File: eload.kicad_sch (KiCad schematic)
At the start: 23 parts, among them J1 Device Power, J2 Input Power, J3 SWD Header, Q1 TIP122, SW1 RotaryEncoder_Switch, U1 STM32F103C8T6, U2 LM1117DT-3.3, U3 AD8629, U4 MCP4725

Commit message: WIP schematic
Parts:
- added C7, C8: C_Small, symbol Device:C_Small
- added C9: 10uF, symbol Device:C_Polarized_Small
- added R10, R5, R9: 10K, symbol Device:R_Small
- added R6: 90K, symbol Device:R_Small
- added Y1: Crystal, symbol Device:Crystal
- R2: value 330K -> 40K
- R3: value 100K -> 10K
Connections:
- net +3.3V: now also C9.1, R10.1, R9.1
- net GND: now also U1.44 (BOOT0), C7.2, C8.2, C9.2, R5.2
- net SCL: now also R9.2
- net SDA: now also R10.2
- net Vctrl: now also R5.1, R6.1; no longer U4.1 (VOUT)
- net OSC1: now reaches U1.5 (PD0)
- net OSC1: now also C8.1, Y1.1
- net OSC2: now reaches U1.6 (PD1)
- net OSC2: now also C7.1, Y1.2
- new net: R6.2, U4.1 (VOUT)
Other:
- note added: "15V MAX 12bit ADC 1bit/mV = 4.096V 5x attenuation on Vsense (15V to 3V)"
- note added: "1A * 0.1R = 0.1V"
- note added: "1V = 1A 10x attenuation"
- note removed: "15V MAX 12bit ADC 1bit/mV = 4.096V 1:4 division"
- moved on the sheet: C1, C5, C6, U1, U4

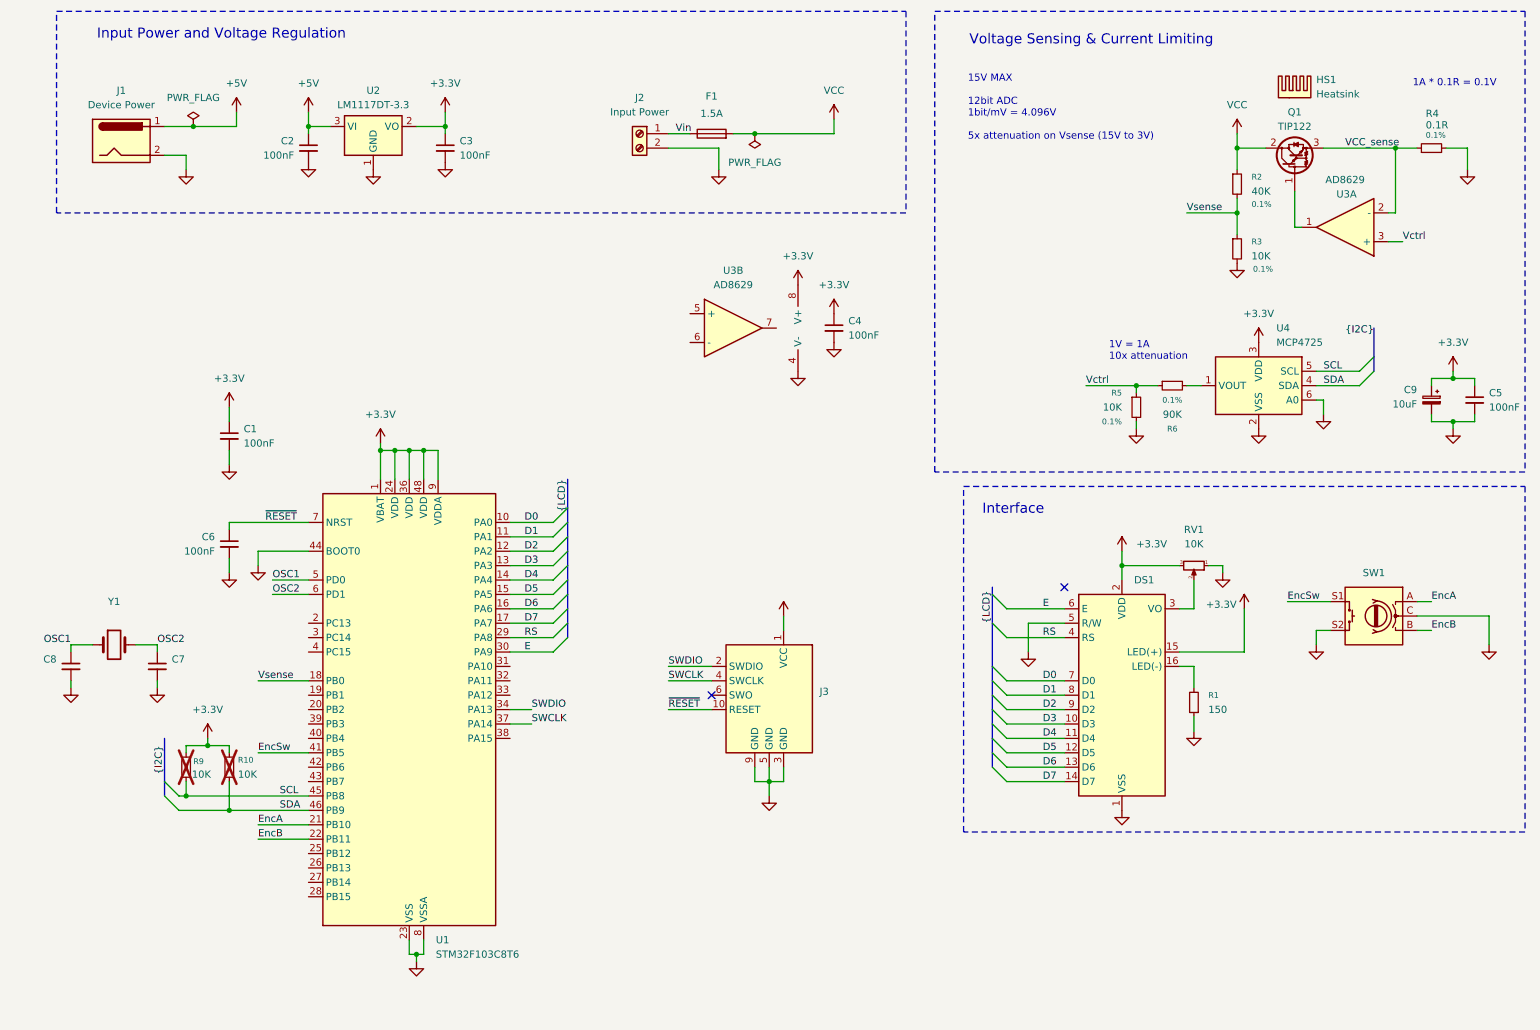
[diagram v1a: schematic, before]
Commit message: Update footprints
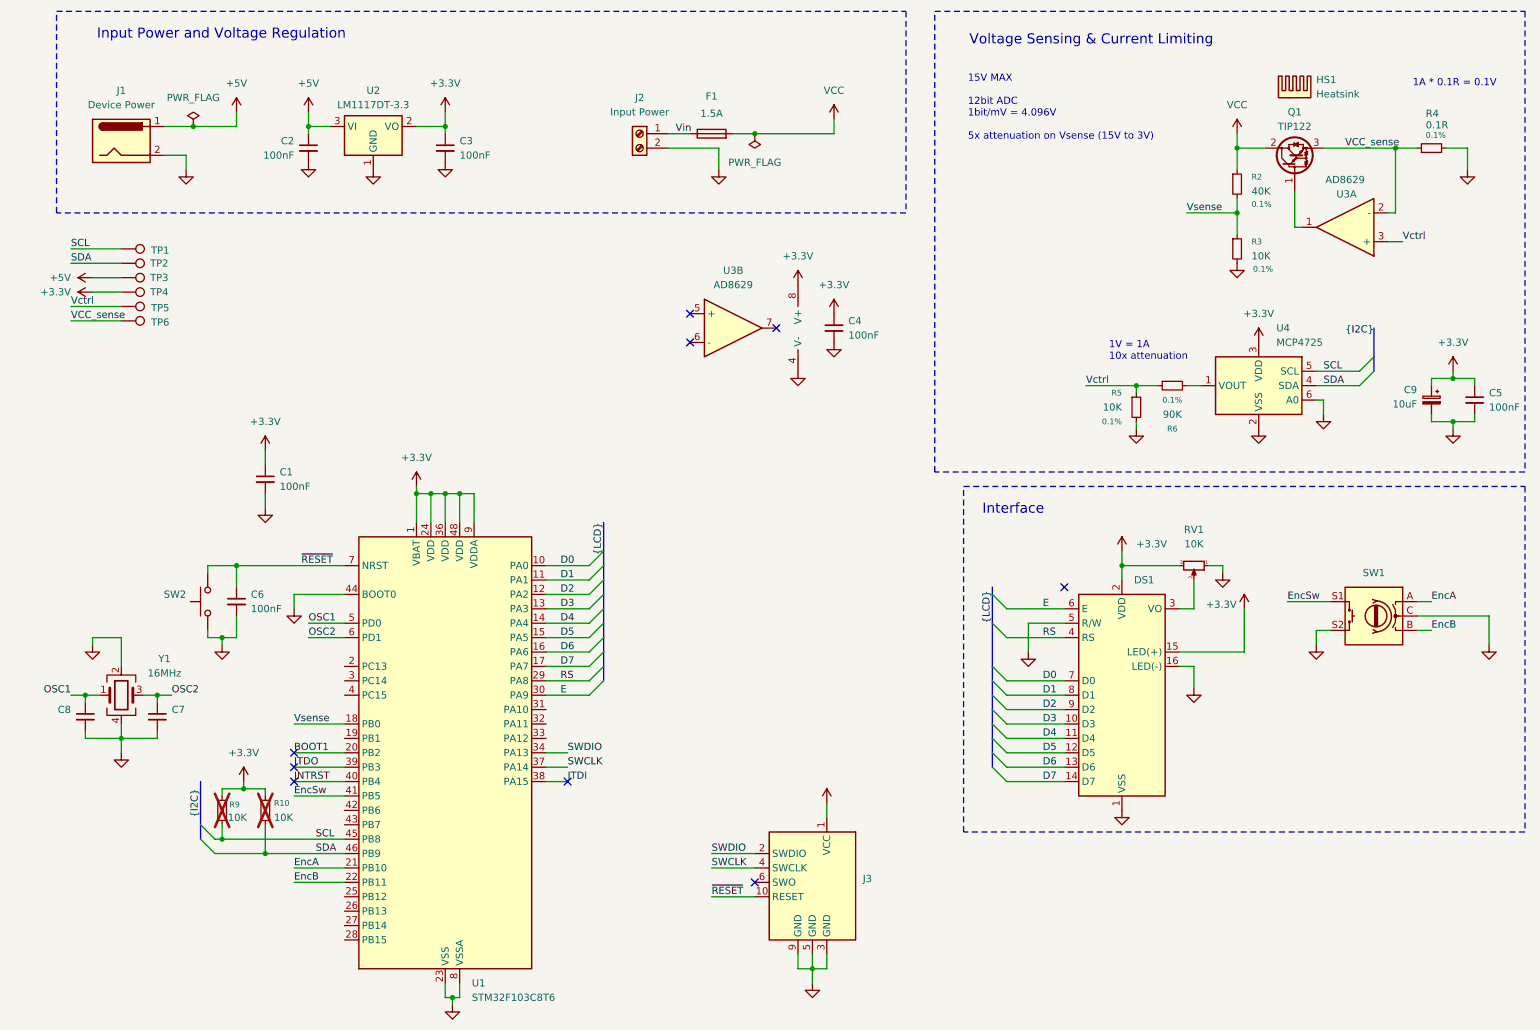
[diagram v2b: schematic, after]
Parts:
- removed R1: 150, symbol Device:R_Small
- removed Y1: Crystal, symbol Device:Crystal
- added SW2: SW_Push, symbol Switch:SW_Push
- added TP1, TP2, TP3, TP4, TP5, TP6: TestPoint, symbol Connector:TestPoint
- added Y1: 16MHz, Crystal:Crystal_SMD_3225-4Pin_3.2x2.5mm_HandSoldering, symbol Device:Crystal_GND24
- C1, C2, C3, C4, C5, C6, C7, C8: footprint (none) -> Capacitor_SMD:C_0805_2012Metric_Pad1.18x1.45mm_HandSolder
- C9: footprint (none) -> Capacitor_Tantalum_SMD:CP_EIA-3216-18_Kemet-A_HandSolder
- U3: footprint (none) -> Package_SO:SOP-8_3.76x4.96mm_P1.27mm; LCSC Part # C47411541 -> C47411543
- U4: LCSC Part # (none) -> C144198
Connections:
- net +3.3V: now also TP4.1
- net +5V: now also TP3.1
- net GND: now also DS1.16 (LED(-)), SW2.1, Y1.2, Y1.4
- net OSC1: now also Y1.1
- net OSC2: now also Y1.3
- net SCL: now also TP1.1
- net SDA: now also TP2.1
- net VCC_sense: now also TP6.1
- net Vctrl: now also TP5.1
- net ~{RESET}: now also SW2.2
- net BOOT1: now reaches U1.20 (PB2)
- net JTDI: now reaches U1.38 (PA15)
- net JTDO: now reaches U1.39 (PB3)
- net JNTRST: now reaches U1.40 (PB4)
- no-connect marks 2 -> 9
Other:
- moved on the sheet: C1, C6, C7, C8, J3, R10, R9, U1

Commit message: WIP
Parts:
- added J3, J6: Conn_01x16_Socket, Connector_JST:JST_XH_B16B-XH-A_1x16_P2.50mm_Vertical, symbol Connector:Conn_01x16_Socket
- added J5: Conn_01x14_Pin, Connector_PinHeader_2.54mm:PinHeader_2x07_P2.54mm_Vertical, symbol Connector:Conn_01x14_Pin
- added TP7: TestPoint, TestPoint:TestPoint_Loop_D1.80mm_Drill1.0mm_Beaded, symbol Connector:TestPoint
- C1: renamed from C8; value C_Small -> 20pF; LCSC Part # (none) -> C149606
- C2: renamed from C7; value C_Small -> 20pF; LCSC Part # (none) -> C149606
- C3: renamed from C6; LCSC Part # (none) -> C49678
- C4: renamed from C1; LCSC Part # (none) -> C49678
- C5: renamed from C2; LCSC Part # (none) -> C49678
- C6: renamed from C3; LCSC Part # (none) -> C49678
- C7: renamed from C4; LCSC Part # (none) -> C49678
- C8: renamed from C9; LCSC Part # (none) -> C110055
- C9: renamed from C5; LCSC Part # (none) -> C49678
- DS1: now left out of the parts list
- J1: footprint Connector_BarrelJack:BarrelJack_SwitchcraftConxall_RAPC10U_Horizontal -> Connector_BarrelJack:BarrelJack_Horizontal; LCSC Part # (none) -> C7498153
- J2: value Input Power -> Input; footprint (none) -> TerminalBlock_CUI:TerminalBlock_CUI_TB007-508-02_1x02_P5.08mm_Horizontal; LCSC Part # (none) -> C8465
- Q1: LCSC Part # C16283 -> C3816270
- R1: renamed from R9; footprint (none) -> Resistor_SMD:R_0805_2012Metric_Pad1.20x1.40mm_HandSolder; LCSC Part # (none) -> C110775
- R2: renamed from R10; footprint (none) -> Resistor_SMD:R_0805_2012Metric_Pad1.20x1.40mm_HandSolder; LCSC Part # (none) -> C110775
- R3: renamed from R5; footprint (none) -> Resistor_SMD:R_0805_2012Metric_Pad1.20x1.40mm_HandSolder; LCSC Part # (none) -> C110775
- R4: renamed from R6; footprint (none) -> Resistor_SMD:R_0805_2012Metric_Pad1.20x1.40mm_HandSolder
- R5: renamed from R2; footprint (none) -> Resistor_SMD:R_0805_2012Metric_Pad1.20x1.40mm_HandSolder; LCSC Part # (none) -> C865475
- R6: renamed from R3; footprint (none) -> Resistor_SMD:R_0805_2012Metric_Pad1.20x1.40mm_HandSolder; LCSC Part # (none) -> C110775
- R7: renamed from R4; footprint (none) -> Resistor_SMD:R_1206_3216Metric_Pad1.30x1.75mm_HandSolder; LCSC Part # (none) -> C7467250
- RV1: footprint (none) -> Potentiometer_THT:Potentiometer_Bourns_3266W_Vertical; LCSC Part # (none) -> C49241482
- SW2: renamed from SW1; footprint (none) -> Rotary_Encoder:RotaryEncoder_Bourns_Vertical_PEC12R-3x17F-Sxxxx; LCSC Part # (none) -> C5331618
- TP1, TP2, TP3, TP4, TP5, TP6: footprint (none) -> TestPoint:TestPoint_Pad_D1.5mm
- U1: renamed from U2; footprint Package_TO_SOT_SMD:TO-252-2 -> Package_TO_SOT_SMD:SOT-223; LCSC Part # (none) -> C126027
- renumbered J3 to J4, SW2 to SW1, U1 to U2
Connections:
- net +3.3V: now also J3.16 (Pin_16), J6.16 (Pin_16)
- net D0: now also J3.15 (Pin_15), J6.15 (Pin_15)
- net D1: now also J3.14 (Pin_14), J6.14 (Pin_14)
- net D2: now also J3.13 (Pin_13), J6.13 (Pin_13)
- net D3: now also J3.12 (Pin_12), J6.12 (Pin_12)
- net D4: now also J3.11 (Pin_11), J6.11 (Pin_11)
- net D5: now also J3.10 (Pin_10), J6.10 (Pin_10)
- net D6: now also J3.9 (Pin_9), J6.9 (Pin_9)
- net D7: now also J3.8 (Pin_8), J6.8 (Pin_8)
- net E: now also J3.7 (Pin_7), J6.7 (Pin_7)
- net EncA: now also J3.3 (Pin_3), J6.3 (Pin_3)
- net EncB: now also J3.2 (Pin_2), J6.2 (Pin_2)
- net EncSw: now also J3.4 (Pin_4), J6.4 (Pin_4)
- net GND: now also J3.1 (Pin_1), J5.1 (Pin_1), J6.1 (Pin_1), TP7.1
- net RS: now also J3.6 (Pin_6), J6.6 (Pin_6)
- net PB1: now reaches U2.19 (PB1)
- net PB1: now also J5.8 (Pin_8)
- net PC13: now reaches U2.2 (PC13)
- net PC13: now also J5.5 (Pin_5)
- net PB12: now reaches U2.25 (PB12)
- net PB12: now also J5.11 (Pin_11)
- net PB13: now reaches U2.26 (PB13)
- net PB13: now also J5.12 (Pin_12)
- net PB14: now reaches U2.27 (PB14)
- net PB14: now also J5.13 (Pin_13)
- net PB15: now reaches U2.28 (PB15)
- net PB15: now also J5.14 (Pin_14)
- net PC14: now reaches U2.3 (PC14)
- net PC14: now also J5.6 (Pin_6)
- net PA10: now reaches U2.31 (PA10)
- net PA10: now also J5.4 (Pin_4)
- net PA11: now reaches U2.32 (PA11)
- net PA11: now also J5.3 (Pin_3)
- net PA12: now reaches U2.33 (PA12)
- net PA12: now also J5.2 (Pin_2)
- net PC15: now reaches U2.4 (PC15)
- net PC15: now also J5.7 (Pin_7)
- net PB6: now reaches U2.42 (PB6)
- net PB6: now also J5.9 (Pin_9)
- net PB7: now reaches U2.43 (PB7)
- net PB7: now also J5.10 (Pin_10)
- no-connect marks 9 -> 10
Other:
- moved on the sheet: DS1, RV1, SW2, TP1, TP2, TP3, TP4, TP5, TP6

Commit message: WIP
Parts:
- F1: footprint (none) -> Resistor_THT:R_Axial_DIN0204_L3.6mm_D1.6mm_P7.62mm_Horizontal
- HS1: LCSC Part # (none) -> C4657
- J3, J6: value Conn_01x16_Socket -> JST Header; LCSC Part # (none) -> C158022
- J5: value Conn_01x14_Pin -> ~; LCSC Part # (none) -> C41413844
- R4: value 90K -> 89.8K; LCSC Part # (none) -> C865684
- U2: value STM32F103C8T6 -> STM32F103CBT6; LCSC Part # (none) -> C8734
- U3: footprint Package_SO:SOP-8_3.76x4.96mm_P1.27mm -> Package_SO:JEITA_SOIC-8_3.9x4.9mm_P1.27mm; LCSC Part # C47411543 -> C653045
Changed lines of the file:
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@@
 			)
 		)
-		(property "Datasheet" "~"
+		(property "Datasheet" "https://www.lcsc.com/datasheet/C4657.pdf"
 			(at 236.5248 33.02 0)
 			(effects
@@
 			)
 		)
+		(property "LCSC Part #" "C4657"
+			(at 236.22 33.02 0)
+			(effects
+				(font
+					(size 1.27 1.27)
+				)
+				(hide yes)
+			)
+		)
 		(instances
 			(project ""
@@
 			)
 		)
-		(property "Value" "Conn_01x16_Socket"
+		(property "Value" "JST Header"
 			(at 146.05 124.4599 0)
 			(effects
@@
 			)
 		)
-		(property "Datasheet" "~"
+		(property "Datasheet" "https://www.lcsc.com/datasheet/C158022.pdf"
 			(at 144.78 121.92 0)
 			(effects
@@
 			)
 		)
+		(property "LCSC Part #" "C158022"
+			(at 144.78 121.92 0)
+			(effects
+				(font
+					(size 1.27 1.27)
+				)
+				(hide yes)
+			)
+		)
 		(pin "2"
 		)
@@
 			)
 		)
-		(property "Value" "STM32F103C8T6"
+		(property "Value" "STM32F103CBT6"
 			(at 91.0433 191.77 0)
 			(effects
@@
 			)
 		)
+		(property "LCSC Part #" "C8734"
+			(at 86.36 148.59 0)
+			(effects
+				(font
+					(size 1.27 1.27)
+				)
+				(hide yes)
+			)
+		)
 		(pin "38"
 		)
@@
 			)
 		)
-		(property "Footprint" "Package_SO:SOP-8_3.76x4.96mm_P1.27mm"
+		(property "Footprint" "Package_SO:JEITA_SOIC-8_3.9x4.9mm_P1.27mm"
 			(at 137.16 73.66 0)
 			(effects
@@
 			)
 		)
-		(property "Datasheet" "https://www.lcsc.com/datasheet/C47411543.pdf"
+		(property "Datasheet" "https://www.analog.com/media/en/technical-documentation/data-sheets/ad8628_8629_8630.pdf"
 			(at 137.16 73.66 0)
 			(effects
@@
 			)
 		)
-		(property "LCSC Part #" "C47411543"
+		(property "LCSC Part #" "C653045"
 			(at 137.16 73.66 0)
 			(effects
@@
 			)
 		)
-		(property "Footprint" "Package_SO:SOP-8_3.76x4.96mm_P1.27mm"
+		(property "Footprint" "Package_SO:JEITA_SOIC-8_3.9x4.9mm_P1.27mm"
 			(at 151.13 73.66 0)
 			(effects
@@
 			)
 		)
-		(property "Datasheet" "https://www.lcsc.com/datasheet/C47411543.pdf"
+		(property "Datasheet" "https://www.analog.com/media/en/technical-documentation/data-sheets/ad8628_8629_8630.pdf"
 			(at 151.13 73.66 0)
 			(effects
@@
 			)
 		)
-		(property "LCSC Part #" "C47411543"
+		(property "LCSC Part #" "C653045"
 			(at 151.13 73.66 0)
 			(effects
@@
 			)
 		)
-		(property "Footprint" "Package_SO:SOP-8_3.76x4.96mm_P1.27mm"
+		(property "Footprint" "Package_SO:JEITA_SOIC-8_3.9x4.9mm_P1.27mm"
 			(at 245.11 55.88 0)
 			(effects
@@
 			)
 		)
-		(property "Datasheet" "https://www.lcsc.com/datasheet/C47411543.pdf"
+		(property "Datasheet" "https://www.analog.com/media/en/technical-documentation/data-sheets/ad8628_8629_8630.pdf"
 			(at 245.11 55.88 0)
 			(effects
@@
 			)
 		)
-		(property "LCSC Part #" "C47411543"
+		(property "LCSC Part #" "C653045"
 			(at 245.11 55.88 0)
 			(effects
@@
 			)
 		)
-		(property "Value" "Conn_01x14_Pin"
+		(property "Value" "~"
 			(at 166.37 123.1899 0)
 			(effects
@@
 			)
 		)
+		(property "LCSC Part #" "C41413844"
+			(at 165.1 123.19 0)
+			(effects
+				(font
+					(size 1.27 1.27)
+				)
+				(hide yes)
+			)
+		)
 		(pin "2"
 		)
@@
 			)
 		)
-		(property "Footprint" ""
+		(property "Footprint" "Resistor_THT:R_Axial_DIN0204_L3.6mm_D1.6mm_P7.62mm_Horizontal"
 			(at 133.35 41.148 90)
 			(effects
@@
 			)
 		)
-		(property "Value" "Conn_01x16_Socket"
+		(property "Value" "JST Header"
 			(at 265.43 142.2399 0)
 			(effects
@@
 			)
 		)
+		(property "LCSC Part #" "C158022"
+			(at 264.16 139.7 0)
+			(effects
+				(font
+					(size 1.27 1.27)
+				)
+				(hide yes)
+			)
+		)
 		(pin "2"
 		)
@@
 			)
 		)
-		(property "Datasheet" "https://www.lcsc.com/datasheet/C865475.pdf"
+		(property "Datasheet" "https://www.lcsc.com/datasheet/C865684.pdf"
 			(at 226.06 48.26 0)
 			(effects
@@
 			)
 		)
-		(property "Value" "90K"
+		(property "Value" "89.8K"
 			(at 214.63 88.9 90)
 			(effects
@@
 			)
 		)
+		(property "LCSC Part #" "C865684"
+			(at 214.63 83.82 90)
+			(effects
+				(font
+					(size 1.27 1.27)
+				)
+				(hide yes)
+			)
+		)

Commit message: Updates in a schematics
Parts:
- J3: LCSC Part # C158022 -> C158018
- J4: LCSC Part # (none) -> C5665
- J5, SW1, TP1, TP2, TP3, TP4, TP5, TP6, TP7: now left out of the parts list
- Q1: LCSC Part # C3816270 -> C16283
- U2: LCSC Part # C8734 -> C8304
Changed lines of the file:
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@@
 			)
 		)
-		(property "Datasheet" "https://www.lcsc.com/datasheet/C158022.pdf"
+		(property "Datasheet" "https://www.lcsc.com/datasheet/C158018.pdf"
 			(at 144.78 121.92 0)
 			(effects
@@
 			)
 		)
-		(property "LCSC Part #" "C158022"
+		(property "LCSC Part #" "C158018"
 			(at 144.78 121.92 0)
 			(effects
@@
 			)
 		)
-		(property "LCSC Part #" "C8734"
+		(property "LCSC Part #" "C8304"
 			(at 86.36 148.59 0)
 			(effects
@@
 		(unit 1)
 		(exclude_from_sim no)
-		(in_bom yes)
+		(in_bom no)
 		(on_board yes)
 		(dnp no)
@@
 		(unit 1)
 		(exclude_from_sim no)
-		(in_bom yes)
+		(in_bom no)
 		(on_board yes)
 		(dnp no)
@@
 		(unit 1)
 		(exclude_from_sim no)
-		(in_bom yes)
-		(on_board yes)
+		(in_bom no)
+		(on_board no)
 		(dnp no)
 		(fields_autoplaced yes)
@@
 		(unit 1)
 		(exclude_from_sim no)
-		(in_bom yes)
+		(in_bom no)
 		(on_board yes)
 		(dnp no)
@@
 			)
 		)
-		(property "LCSC Part #" "C3816270"
+		(property "LCSC Part #" "C16283"
 			(at 236.22 44.45 90)
 			(effects
@@
 		(unit 1)
 		(exclude_from_sim no)
-		(in_bom yes)
+		(in_bom no)
 		(on_board yes)
 		(dnp no)
@@
 		(unit 1)
 		(exclude_from_sim no)
-		(in_bom yes)
+		(in_bom no)
 		(on_board yes)
 		(dnp no)
@@
 		(unit 1)
 		(exclude_from_sim no)
-		(in_bom yes)
+		(in_bom no)
 		(on_board yes)
 		(dnp no)
@@
 		(unit 1)
 		(exclude_from_sim no)
-		(in_bom yes)
+		(in_bom no)
 		(on_board yes)
 		(dnp no)
@@
 			)
 		)
-		(property "Datasheet" "~"
+		(property "Datasheet" "https://www.lcsc.com/datasheet/C158022.pdf"
 			(at 264.16 139.7 0)
 			(effects
@@
 			)
 		)
-		(property "Datasheet" "https://www.lcsc.com/datasheet/C3816270.pdf"
+		(property "Datasheet" ""
 			(at 158.75 162.56 0)
 			(effects
@@
 			)
 		)
+		(property "LCSC Part #" "C5665"
+			(at 158.75 162.56 0)
+			(effects
+				(font
+					(size 1.27 1.27)
+				)
+				(hide yes)
+			)
+		)
 		(pin "3"
 		)
@@
 		(unit 1)
 		(exclude_from_sim no)
-		(in_bom yes)
+		(in_bom no)
 		(on_board yes)
 		(dnp no)
